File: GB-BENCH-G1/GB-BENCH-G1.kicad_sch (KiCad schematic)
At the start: 98 parts, among them J1 BARREL_JACK, J10 CONN_01X06, J11 CONN_02X16, J12 CONN_01X06, J13 Conn_GameBoy_Cartridge_Slot, J14 CONN_01X05, J2 Conn_Molex_19708, J3 CONN_02X08, J4 CONN_02X08, J7 CONN_02X05, J8 CONN_02X13, J9 CONN_01X08, SW1 SW_SPST, U1 LC4256ZE-XXTN100, U2 MCP1703A-1802/MB, U3 MCP1703A-3302/MB, U4 MCP1703A-5002/MB, U5 LC4256ZE-XXTN100, U6 GameBoy_SRAM_64K, U7 GameBoy_SRAM_64K, U8 GameBoy_CPU_DMG-SGB, X1 XO32

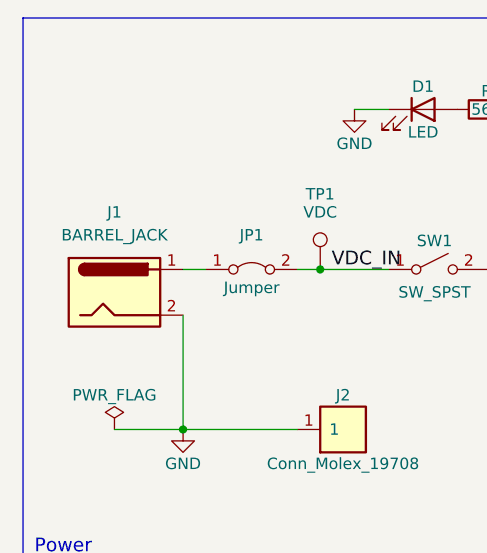
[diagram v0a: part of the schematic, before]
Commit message: Upgrade projects to KiCad 7
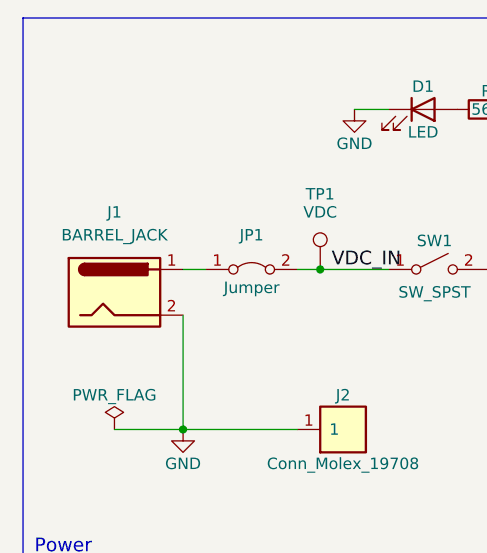
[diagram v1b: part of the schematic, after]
